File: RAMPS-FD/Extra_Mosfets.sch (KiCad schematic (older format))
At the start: 14 parts, among them P901 D11_EXT, P902 D2_EXT, Q901 2N7002, Q902 2N7002

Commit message: RAMPS-FD latest updates
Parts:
- removed R901, R902: 10k, ~, symbol R
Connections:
- net D11-FET5 renamed FET5_BUF
- net D2-FET6 renamed FET6_BUF
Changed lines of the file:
@@
 Sheet 9 9
 Title ""
-Date "22 sep 2013"
+Date "23 sep 2013"
 Rev ""
 Comp ""
@@
 $EndComp
 $Comp
-L GNDPWR #PWR0113
+L GNDPWR #PWR0114
 U 1 1 523E5FF8
 P 3500 3200
-F 0 "#PWR0113" H 3500 3250 40  0001 C CNN
+F 0 "#PWR0114" H 3500 3250 40  0001 C CNN
 F 1 "GNDPWR" H 3500 3120 40  0000 C CNN
 F 2 "" H 3500 3200 60  0001 C CNN
@@
 $EndComp
 Text GLabel 1450 2400 0    60   Input ~ 0
-D11-FET5
-$Comp
-L +12P #PWR0114
+FET5_BUF
+$Comp
+L +12P #PWR0115
 U 1 1 523E6026
 P 3500 850
-F 0 "#PWR0114" H 3500 820 30  0001 C CNN
+F 0 "#PWR0115" H 3500 820 30  0001 C CNN
 F 1 "+12P" H 3500 950 30  0000 C CNN
 F 2 "" H 3500 850 60  0000 C CNN
@@
 Text Label 4000 2050 0    50   ~ 0
 P_FET5
-$Comp
-L R R901
-U 1 1 523E661E
-P 2000 2850
-F 0 "R901" V 2080 2850 40  0000 C CNN
-F 1 "10k" V 2007 2851 40  0000 C CNN
-F 2 "~" V 1930 2850 30  0000 C CNN
-F 3 "~" H 2000 2850 30  0000 C CNN
-	1    2000 2850
-	1    0    0    -1
-$EndComp
 $Comp
 L R R903
@@
 	2250 2400 1450 2400
 Wire Wire Line
-	2000 2600 2000 2400
-Connection ~ 2000 2400
-Wire Wire Line
 	3200 2400 2750 2400
-$Comp
-L GND #PWR0115
-U 1 1 523E6671
-P 2000 3250
-F 0 "#PWR0115" H 2000 3250 30  0001 C CNN
-F 1 "GND" H 2000 3180 30  0001 C CNN
-F 2 "" H 2000 3250 60  0000 C CNN
-F 3 "" H 2000 3250 60  0000 C CNN
-	1    2000 3250
-	1    0    0    -1
-$EndComp
-Wire Wire Line
-	2000 3250 2000 3100
 Connection ~ 3500 4200
 Wire Wire Line
@@
 $EndComp
 Text GLabel 1450 5600 0    60   Input ~ 0
-D2-FET6
+FET6_BUF
 $Comp
 L +12P #PWR0117
@@
 P_FET6
 $Comp
-L R R902
-U 1 1 523E66D1
-P 2000 6050
-F 0 "R902" V 2080 6050 40  0000 C CNN
-F 1 "10k" V 2007 6051 40  0000 C CNN
-F 2 "~" V 1930 6050 30  0000 C CNN
-F 3 "~" H 2000 6050 30  0000 C CNN
-	1    2000 6050
-	1    0    0    -1
-$EndComp
-$Comp
 L R R904
 U 1 1 523E66D7
@@
 $EndComp
 Wire Wire Line
-	2250 5600 1450 5600
-Wire Wire Line
-	2000 5800 2000 5600
+	1450 5600 2250 5600
 Connection ~ 2000 5600
 Wire Wire Line
 	3200 5600 2750 5600
-$Comp
-L GND #PWR0118
-U 1 1 523E66E1
-P 2000 6450
-F 0 "#PWR0118" H 2000 6450 30  0001 C CNN
-F 1 "GND" H 2000 6380 30  0001 C CNN
-F 2 "" H 2000 6450 60  0000 C CNN
-F 3 "" H 2000 6450 60  0000 C CNN
-	1    2000 6450
-	1    0    0    -1
-$EndComp
-Wire Wire Line
-	2000 6450 2000 6300
+Connection ~ 2000 2400
 $EndSCHEMATC

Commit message: RAMPS-FD: latest update
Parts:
- removed R903, R904: 10R, ~, symbol R
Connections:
- net FET5_BUF: now also Q901.G
- net FET6_BUF: now also Q902.G
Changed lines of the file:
@@
 Sheet 9 9
 Title ""
-Date "23 sep 2013"
+Date "24 sep 2013"
 Rev ""
 Comp ""
@@
 Text Label 4000 2050 0    50   ~ 0
 P_FET5
-$Comp
-L R R903
-U 1 1 523E662D
-P 2500 2400
-F 0 "R903" V 2580 2400 40  0000 C CNN
-F 1 "10R" V 2507 2401 40  0000 C CNN
-F 2 "~" V 2430 2400 30  0000 C CNN
-F 3 "~" H 2500 2400 30  0000 C CNN
-	1    2500 2400
-	0    -1   -1   0
-$EndComp
-Wire Wire Line
-	2250 2400 1450 2400
-Wire Wire Line
-	3200 2400 2750 2400
+Wire Wire Line
+	3200 2400 1450 2400
 Connection ~ 3500 4200
 Wire Wire Line
@@
 Text Label 4000 5250 0    50   ~ 0
 P_FET6
-$Comp
-L R R904
-U 1 1 523E66D7
-P 2500 5600
-F 0 "R904" V 2580 5600 40  0000 C CNN
-F 1 "10R" V 2507 5601 40  0000 C CNN
-F 2 "~" V 2430 5600 30  0000 C CNN
-F 3 "~" H 2500 5600 30  0000 C CNN
-	1    2500 5600
-	0    -1   -1   0
-$EndComp
-Wire Wire Line
-	1450 5600 2250 5600
-Connection ~ 2000 5600
-Wire Wire Line
-	3200 5600 2750 5600
-Connection ~ 2000 2400
+Wire Wire Line
+	3200 5600 1450 5600
 $EndSCHEMATC

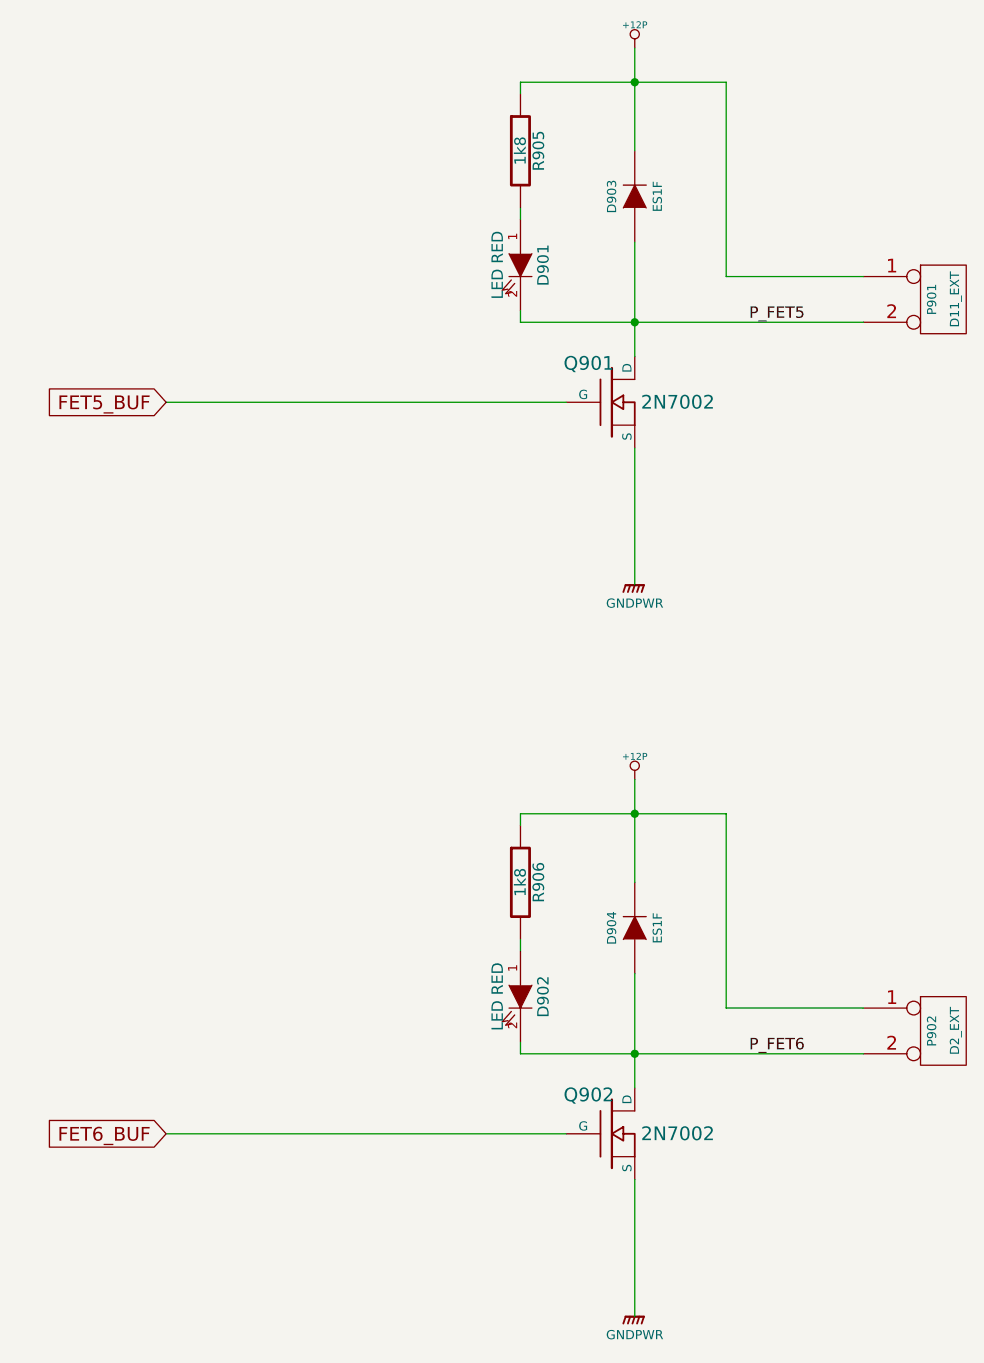
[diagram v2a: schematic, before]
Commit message: RAMPS-FD: update schematic, layout
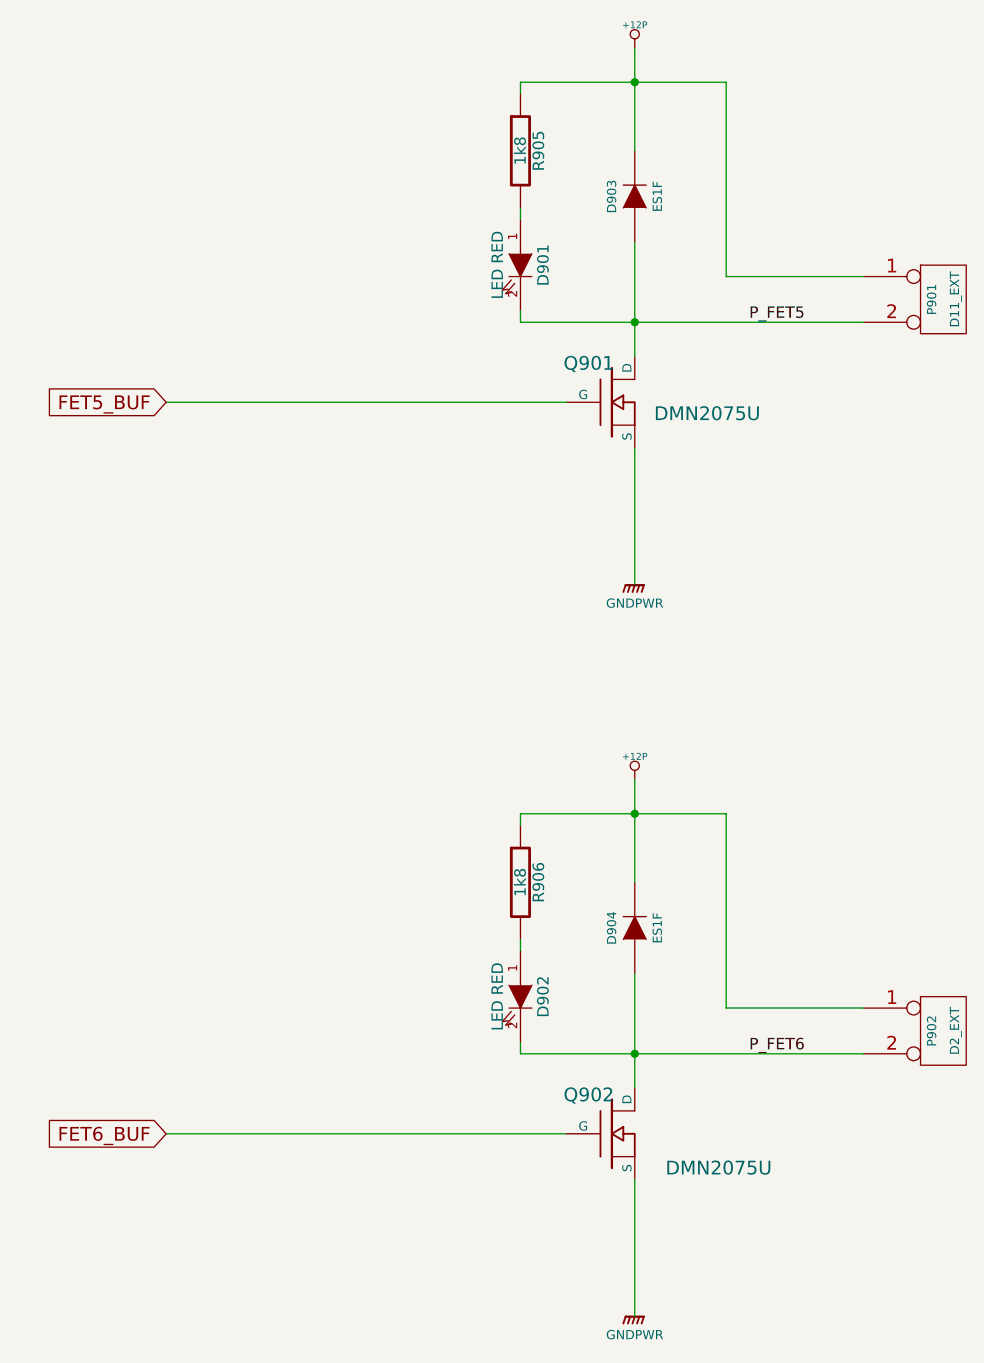
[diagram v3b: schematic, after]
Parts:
- Q901, Q902: value 2N7002 -> DMN2075U
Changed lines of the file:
@@
 Sheet 9 9
 Title ""
-Date "24 sep 2013"
+Date "26 sep 2013"
 Rev ""
 Comp ""
@@
 P 3400 2400
 F 0 "Q901" H 3410 2570 60  0000 R CNN
-F 1 "2N7002" H 3850 2400 60  0000 R CNN
+F 1 "DMN2075U" H 4050 2350 60  0000 R CNN
 F 2 "" H 3400 2400 60  0001 C CNN
 F 3 "" H 3400 2400 60  0001 C CNN
@@
 P 3400 5600
 F 0 "Q902" H 3410 5770 60  0000 R CNN
-F 1 "2N7002" H 3850 5600 60  0000 R CNN
+F 1 "DMN2075U" H 4100 5450 60  0000 R CNN
 F 2 "" H 3400 5600 60  0001 C CNN
 F 3 "" H 3400 5600 60  0001 C CNN

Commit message: RAMPS-FD: version 1 Rev A
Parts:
- P901: value D11_EXT -> D12
- P902: value D2_EXT -> D2
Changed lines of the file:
@@
 Sheet 9 9
 Title ""
-Date "26 sep 2013"
+Date "3 oct 2013"
 Rev ""
 Comp ""
@@
 $EndComp
 $Comp
-L GNDPWR #PWR0114
+L GNDPWR #PWR0115
 U 1 1 523E5FF8
 P 3500 3200
-F 0 "#PWR0114" H 3500 3250 40  0001 C CNN
+F 0 "#PWR0115" H 3500 3250 40  0001 C CNN
 F 1 "GNDPWR" H 3500 3120 40  0000 C CNN
 F 2 "" H 3500 3200 60  0001 C CNN
@@
 P 4850 1950
 F 0 "P901" V 4800 1950 40  0000 C CNN
-F 1 "D11_EXT" V 4900 1950 40  0000 C CNN
+F 1 "D12" V 4900 1950 40  0000 C CNN
 F 2 "" H 4850 1950 60  0001 C CNN
 F 3 "" H 4850 1950 60  0001 C CNN
@@
 FET5_BUF
 $Comp
-L +12P #PWR0115
+L +12P #PWR0116
 U 1 1 523E6026
 P 3500 850
-F 0 "#PWR0115" H 3500 820 30  0001 C CNN
+F 0 "#PWR0116" H 3500 820 30  0001 C CNN
 F 1 "+12P" H 3500 950 30  0000 C CNN
 F 2 "" H 3500 850 60  0000 C CNN
@@
 $EndComp
 $Comp
-L GNDPWR #PWR0116
+L GNDPWR #PWR0117
 U 1 1 523E66AB
 P 3500 6400
-F 0 "#PWR0116" H 3500 6450 40  0001 C CNN
+F 0 "#PWR0117" H 3500 6450 40  0001 C CNN
 F 1 "GNDPWR" H 3500 6320 40  0000 C CNN
 F 2 "" H 3500 6400 60  0001 C CNN
@@
 P 4850 5150
 F 0 "P902" V 4800 5150 40  0000 C CNN
-F 1 "D2_EXT" V 4900 5150 40  0000 C CNN
+F 1 "D2" V 4900 5150 40  0000 C CNN
 F 2 "" H 4850 5150 60  0001 C CNN
 F 3 "" H 4850 5150 60  0001 C CNN
@@
 FET6_BUF
 $Comp
-L +12P #PWR0117
+L +12P #PWR0118
 U 1 1 523E66CA
 P 3500 4050
-F 0 "#PWR0117" H 3500 4020 30  0001 C CNN
+F 0 "#PWR0118" H 3500 4020 30  0001 C CNN
 F 1 "+12P" H 3500 4150 30  0000 C CNN
 F 2 "" H 3500 4050 60  0000 C CNN
